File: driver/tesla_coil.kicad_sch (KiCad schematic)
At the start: 39 parts, among them J1 Screw_Terminal_01x02, J2 Screw_Terminal_01x02, J3 Screw_Terminal_01x02, Q1 FDD8424H, Q2 FDD8424H, Q3 FDD8424H, Q4 FDD8424H, U1 uA7805, U2 L7812, U3 UCC27523D, U4 UCC27523D

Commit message: prelim driver sch done
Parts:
- added C19, C20, C21, C23, C24: 100nF, symbol Device:C_Small
- added C22: C_Small, symbol Device:C_Small
- added C25: 1n, symbol Device:C_Small
- added D10, D11, D12, D13, D14, D15, D16, D17: D, symbol Device:D
- added D18, D19, D9: LED, symbol Device:LED
- added D5, D6: D_Zener, symbol Device:D_Zener
- added D7, D8: D_Schottky, symbol Device:D_Schottky
- added J4: PHASE_ADJ, symbol Connector_Generic:Conn_02x03_Odd_Even
- added J5, J6: Screw_Terminal_01x02, symbol Connector:Screw_Terminal_01x02
- added R10, R13, R14, R16, R7, R9: 1k, symbol Device:R_US
- added R11: 20k, symbol Device:R_US
- added R12: 10, symbol Device:R_US
- added R15, R8: 470, symbol Device:R_US
- added RV1: 10k, symbol Device:R_Potentiometer_US
- added U5: ~, symbol IFD95OC:IFD95OC
- added U6: 74HC14, symbol 74xx:74HC14
- added U7: 74HC74, symbol 74xx:74HC74
- added U8: 74LS08, symbol 74xx:74LS08
- added U9: LM311, symbol Comparator:LM311
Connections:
- net +5V: now also C19.2, C21.2, C24.2, D12.1 (K), R13.2, R14.1, R16.2, R7.1, R8.2, U5.3 (VCC), U6.14 (VCC), U7.10 (~{S}), U7.12 (D), U7.14 (VCC), U8.14 (VCC), U9.8 (V+)
- net GND: now also C19.1, C21.1, C22.2, C23.1, C24.1, C25.2, D11.2 (A), D18.1 (K), D19.1 (K), D5.2 (A), D7.2 (A), J5.1 (Pin_1), R10.1, RV1.3, U5.1 (GND), U6.7 (GND), U7.2 (D), U7.7 (GND), U8.12, U8.13, U8.7 (GND), U9.1 (GND), U9.4 (V-)
- net at U3.2 (INA): now also U4.2 (INA), J4.1 (Pin_1), J4.6 (Pin_6)
- net at U3.4 (INB): now also U4.4 (INB), J4.2 (Pin_2), J4.5 (Pin_5)
- new net: D10.1 (K), R10.2, U7.11 (C), U8.1
- new net: D18.2 (A), R16.1
- new net: R13.1, RV1.1
- new net: D5.1 (K), D8.1 (K)
- new net: D6.1 (K), D7.1 (K)
- new net: C20.1, D6.2 (A), D8.2 (A), J5.2 (Pin_2)
- new net: U6.2, U6.3
- new net: D10.2 (A), U6.4
- new net: D9.1 (K), R7.2, U5.2 (OUT), U6.1
- new net: D9.2 (A), R8.1
- new net: D16.2 (A), D17.1 (K), J6.1 (Pin_1)
- new net: D15.2 (A), D17.2 (A), R12.2
- new net: C23.2, RV1.2, U9.2 (+)
- new net: D11.1 (K), D12.2 (A), R9.2, U6.5
- new net: U6.6, U6.9, U7.3 (C), U8.9
- new net: C20.2, R9.1
- new net: U6.12, U7.1 (~{R})
- new net: D13.1 (K), R11.2, U6.10, U7.4 (~{S})
- new net: U7.5 (Q), U8.10, U8.4
- new net: U7.9 (Q), U8.2
- new net: U6.11, U8.3
- new net: D14.2 (A), D15.1 (K), J6.2 (Pin_2)
- new net: C22.1, D13.2 (A), R11.1, U6.13
- new net: J4.4 (Pin_4), U8.8
- new net: U6.8, U8.5
- new net: J4.3 (Pin_3), U8.6
- new net: C25.1, R14.2, U7.13 (~{R}), U9.7
- new net: D14.1 (K), D16.1 (K), R12.1, U9.3 (-)
- new net: R15.1, U7.8 (~{Q})
- new net: D19.2 (A), R15.2
- new net: U9.5 (BAL), U9.6 (STRB)
- no-connect marks 0 -> 2
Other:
- note added: "Feedback"
- note added: "GDT 1"
- note added: "GDT 2"
- note added: "Interrupter"
- note added: "Overcurrent detection"
- note added: "Power"
- title: (none) -> Krishna's DRSSTC Driver
- moved on the sheet: C10, C11, C12, C13, C14, C15, C16, C17, C18, C5, C6, C7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

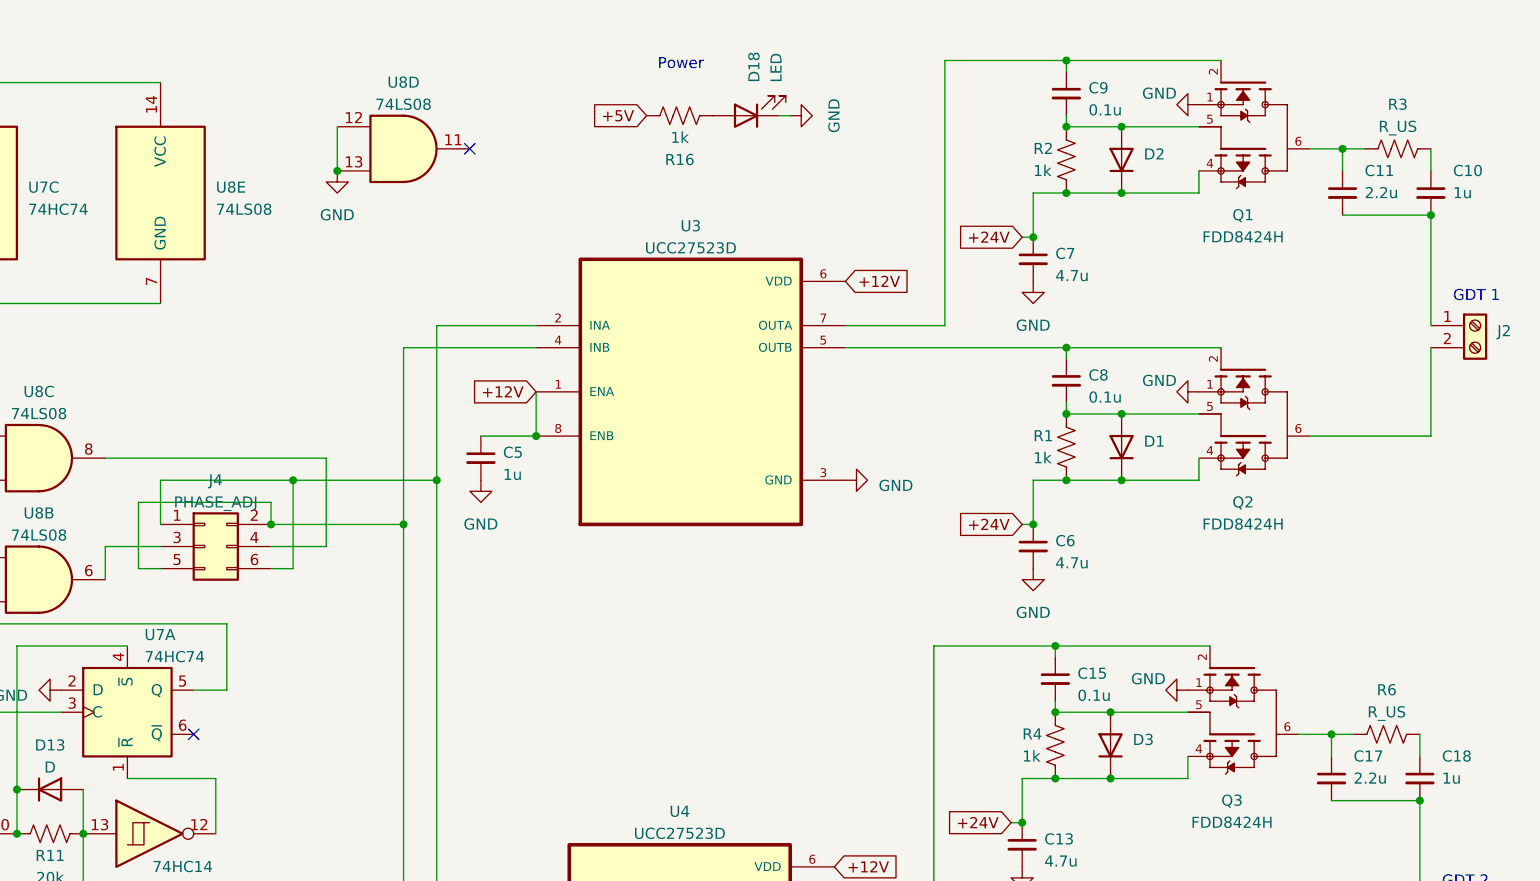
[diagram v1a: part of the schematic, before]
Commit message: finish basic bridge, remove voltage doubler
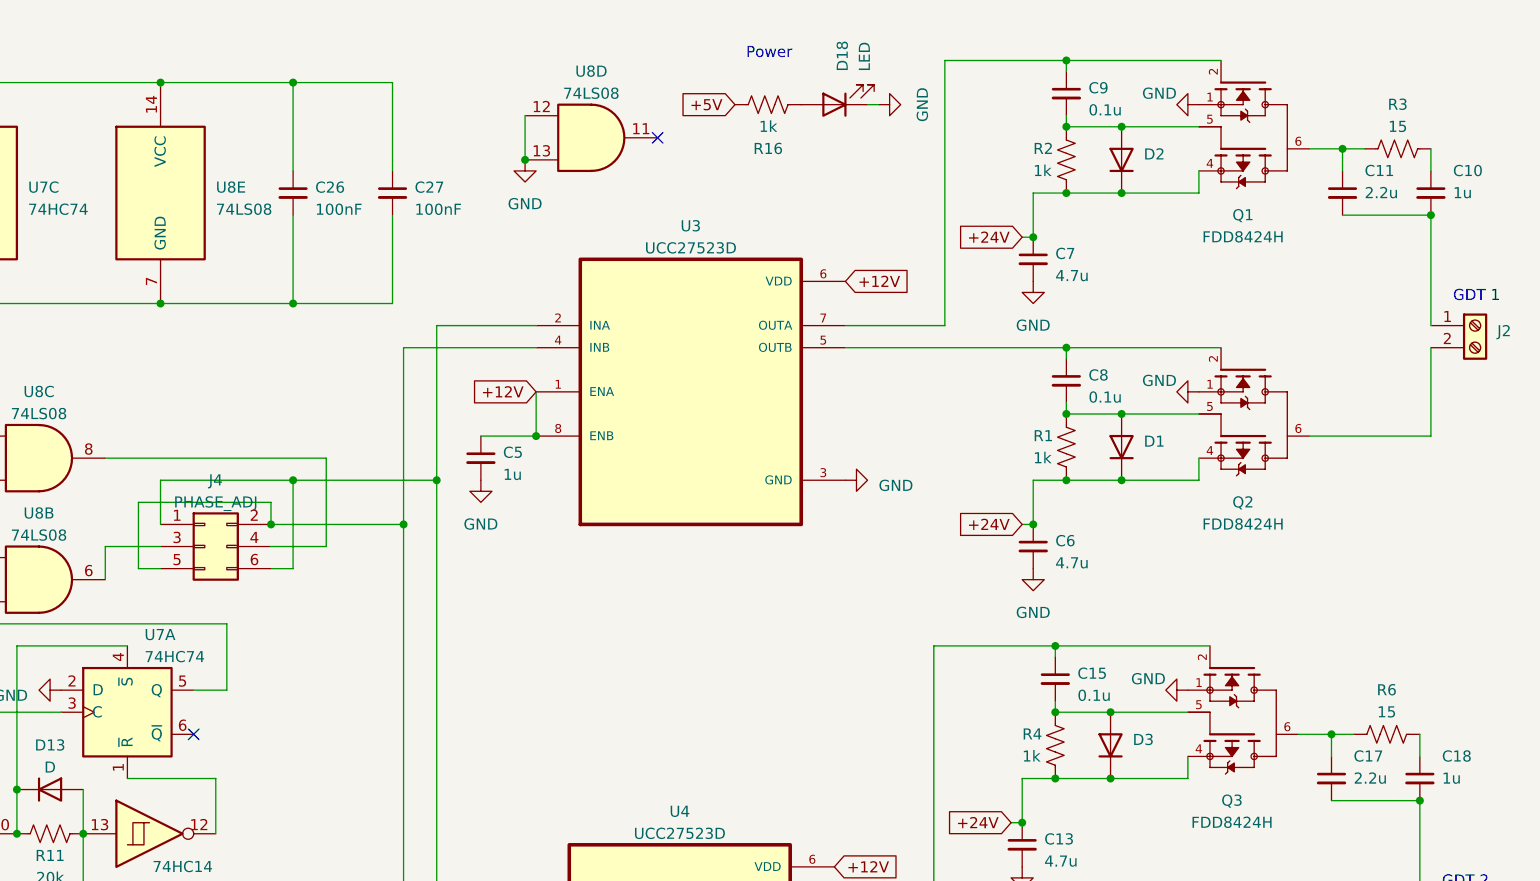
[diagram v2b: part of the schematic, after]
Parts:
- added C26, C27: 100nF, symbol Device:C_Small
- R3, R6: value R_US -> 15
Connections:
- net +5V: now also C26.1, C27.1
- net GND: now also C26.2, C27.2
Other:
- moved on the sheet: D18, R16, U8D

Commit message: bridge footprints done
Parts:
- C22: value C_Small -> 0.1u
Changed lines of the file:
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@@
       (effects (font (size 1.27 1.27)) (justify left))
     )
-    (property "Value" "C_Small" (at 152.4 118.7513 0)
+    (property "Value" "0.1u" (at 152.4 118.7513 0)
       (effects (font (size 1.27 1.27)) (justify left))
     )
